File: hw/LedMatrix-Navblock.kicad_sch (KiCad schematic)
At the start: 38 parts, among them Q4200 DTA114E, Q4201 DTA114E, Q4202 DTA114E, Q4203 DTA114E, Q4204 DTA114E, Q4205 DTC114EE, Q4206 DTC114EE, Q4207 DTC114EE, Q4208 DTC114EE, Q4209 DTC114EE, Q4210 DTC114EE, Q4211 DTC114EE, Q4212 DTC114EE, Q4213 DTC114EE

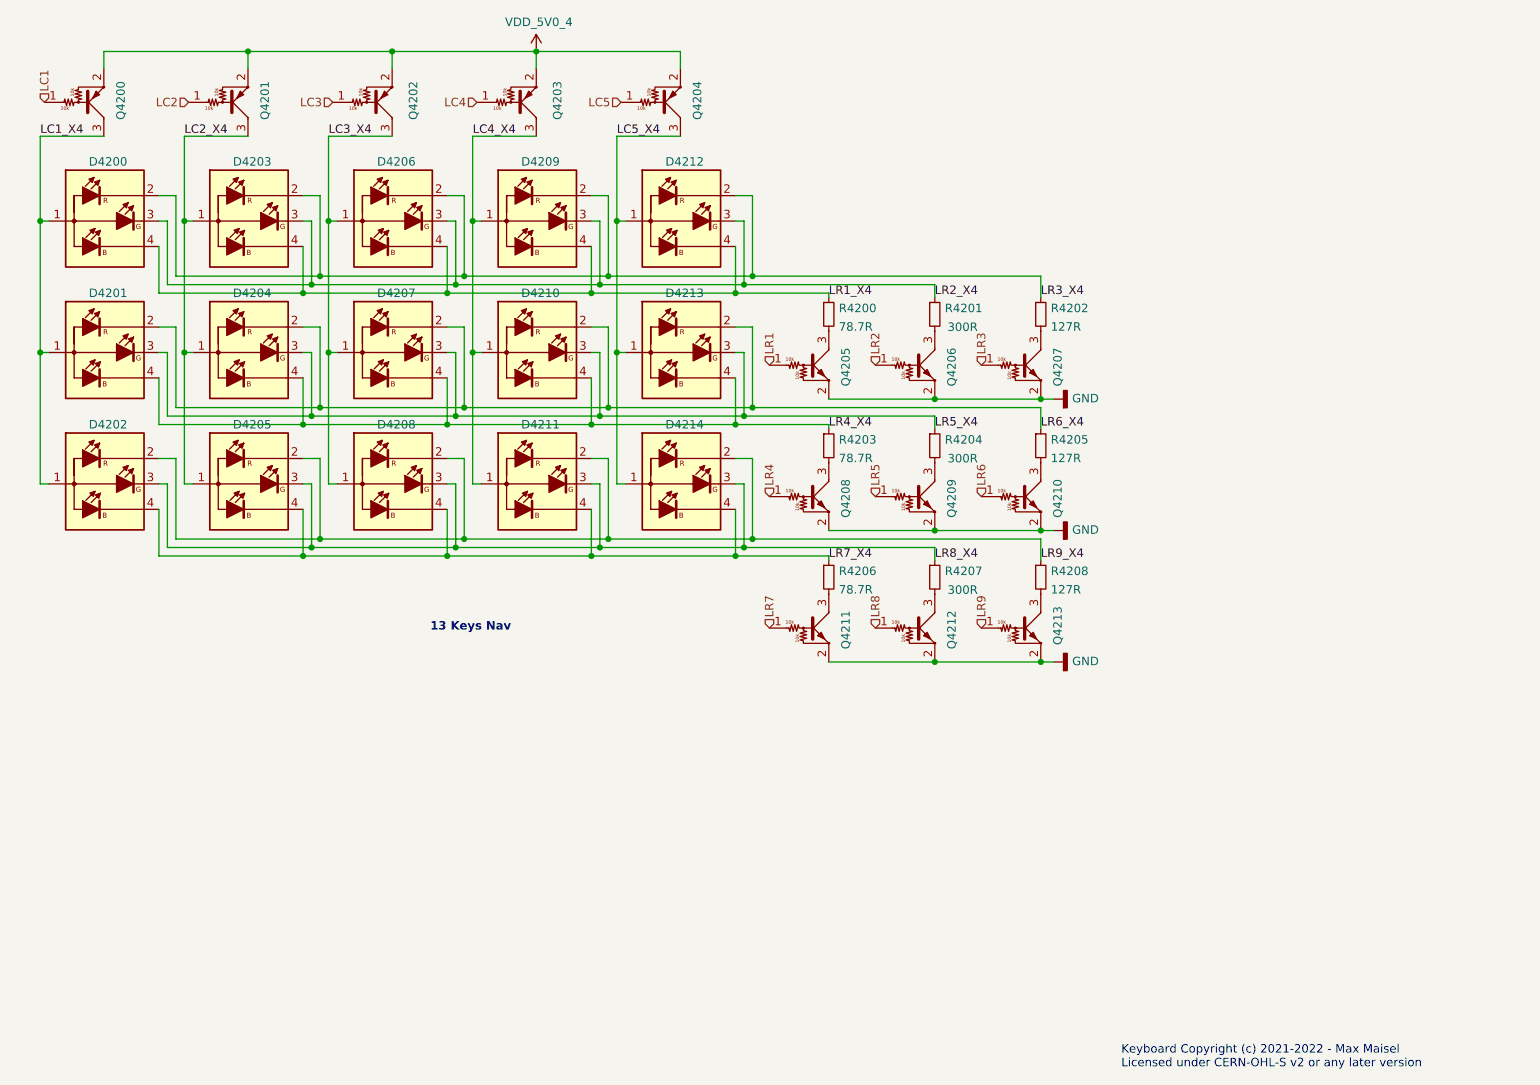
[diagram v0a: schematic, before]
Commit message: Replace LED matrix BJTs with MOSFETs and update PCB.
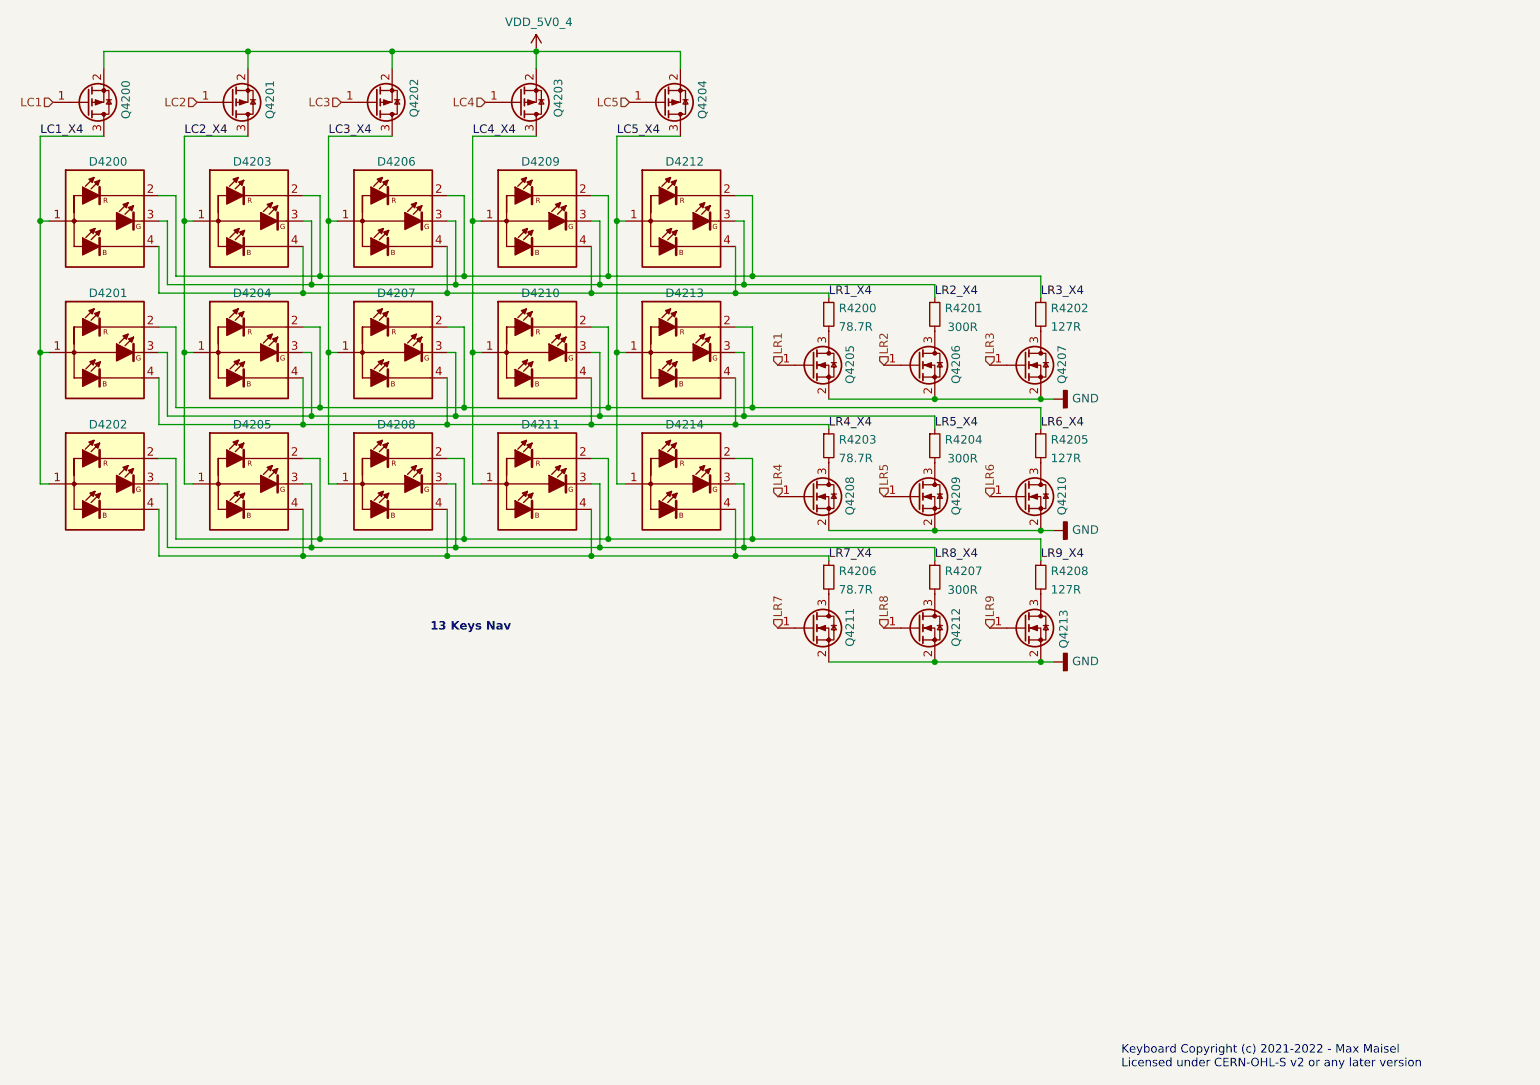
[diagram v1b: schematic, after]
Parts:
- Q4200, Q4201, Q4202, Q4203, Q4204: value DTA114E -> NTA4151P; symbol Keyboard:DTA114E -> Keyboard:NTA4151PT1G; farnell# (none) -> 2317622; mouser# (none) -> 863-NTA4151PT1G
- Q4205, Q4206, Q4207, Q4208, Q4209, Q4210, Q4211, Q4212, Q4213: value DTC114EE -> NTA4153N; symbol Keyboard:DTC114EE -> Keyboard:NTA4153NT1G; farnell# (none) -> 2317621; mouser# 863-DTC114EET1G -> 863-NTA4153NT1G
